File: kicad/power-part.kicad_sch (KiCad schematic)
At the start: 53 parts, among them Q10 BSS84, Q11 BSS123N, Q12 ZXMP10A17GTA, Q2 IPT012N08N5, Q3 IPT012N08N5, Q4 IPT012N08N5, Q5 IPT012N08N5, Q6 IPT012N08N5, Q7 IPT012N08N5, Q8 IPT012N08N5, Q9 IPT012N08N5

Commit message: Update files to KiCad v8
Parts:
- RT1, RT2: LCSC (none) -> C406719

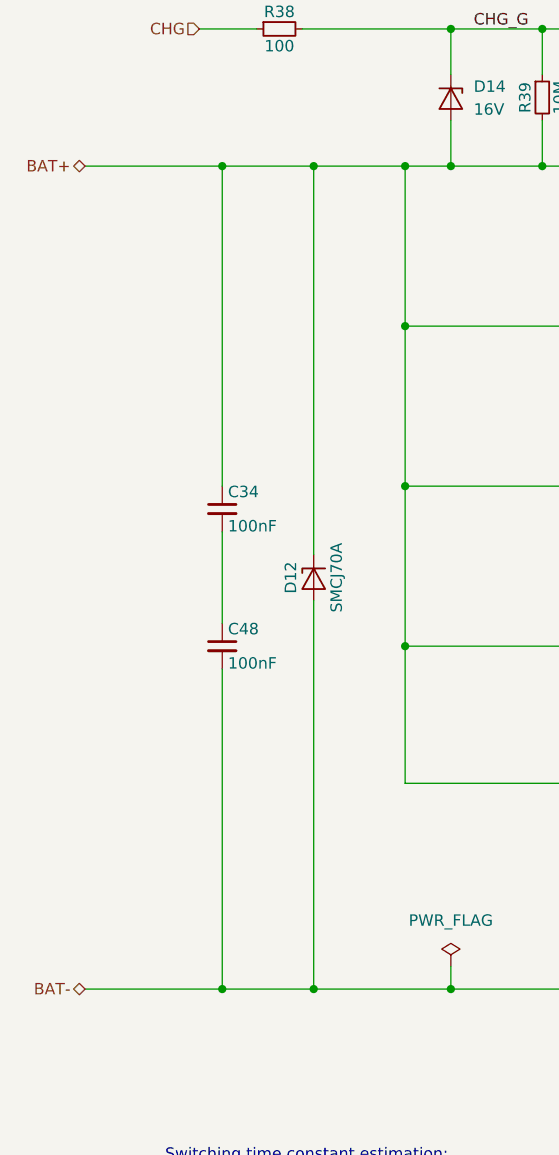
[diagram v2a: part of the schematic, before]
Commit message: changes done by jc-efactory: capacitor integrated, a 10mm SMD electrolitic footprint to test fix for issue #68, update to Kicad V9, rerouting, like the 3V3 plane was removed, now a GND layer as well and had to change a couple of capacitor to be able to fit the changes without any major redesign.
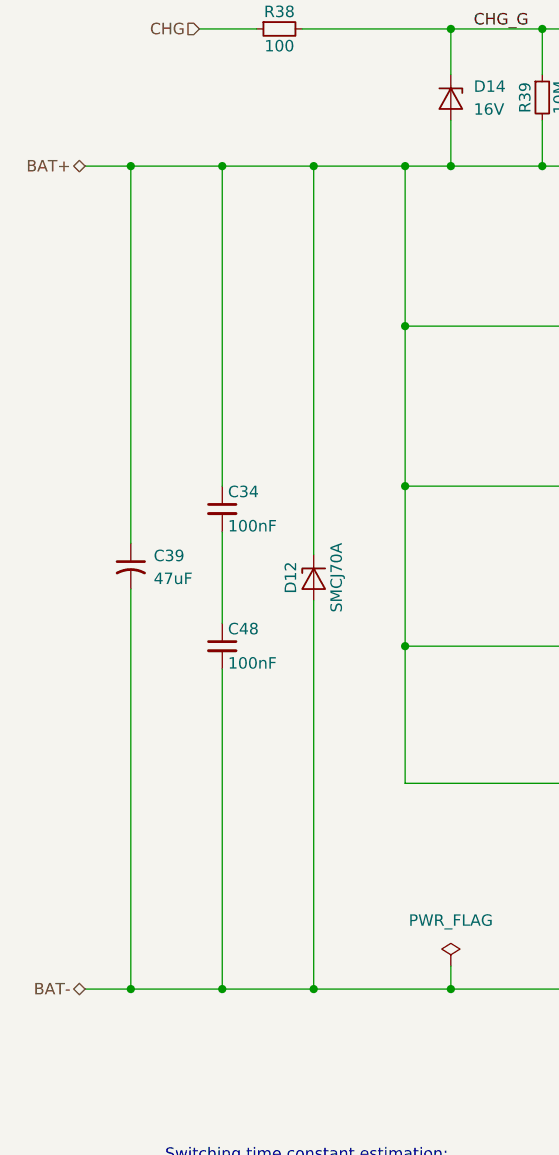
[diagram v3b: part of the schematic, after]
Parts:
- added C39: 47uF, Capacitor_SMD:CP_Elec_10x10, symbol Device:C_Small_US
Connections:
- net BAT+: now also C39.1
- net BAT-: now also C39.2
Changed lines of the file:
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@@
 (kicad_sch
-	(version 20231120)
+	(version 20250114)
 	(generator "eeschema")
-	(generator_version "8.0")
+	(generator_version "9.0")
 	(paper "A4")
 	(title_block
@@
 		(comment 3 "License: CERN-OHL-W")
 	)
+	(text "Protection against\ncharger with \nreversed polarity"
+		(exclude_from_sim no)
+		(at 208.28 26.67 0)
+		(effects
+			(font
+				(size 1.27 1.27)
+			)
+			(justify left bottom)
+		)
+	)
+	(text "Switching time constant estimation:\n- 4x IPT015N10N5 with C_iss = 16nF: 64nF\n- Gate resistor: 47R\n- Time constant: R*C = 3us"
+		(exclude_from_sim no)
+		(at 36.83 185.42 0)
+		(effects
+			(font
+				(size 1.27 1.27)
+			)
+			(justify left bottom)
+		)
+	)
+	(text "MOSFETs and Shunt"
+		(exclude_from_sim no)
+		(at 34.29 33.02 0)
+		(effects
+			(font
+				(size 2.54 2.54)
+			)
+			(justify left bottom)
+		)
+	)
+	(text "Local turn-off \ncircuit for higher\nspeed/current"
+		(exclude_from_sim no)
+		(at 182.88 26.67 0)
+		(effects
+			(font
+				(size 1.27 1.27)
+			)
+			(justify left bottom)
+		)
+	)
+	(text "Bus precharge circuit"
+		(exclude_from_sim no)
+		(at 187.96 86.36 0)
+		(effects
+			(font
+				(size 2.54 2.54)
+			)
+			(justify left bottom)
+		)
+	)
+	(text "Calculations:\n- Peak current: 60V / 40R = 1.5A\n- Time constant for C_bus 5mF: 0.2s\n- Dissipated energy: 9J\n\nShort circuit must be detected and\ninterrupted within <100 ms to\navoid overloading of the resistor.\n\nMax. continuous current: 0.5 A"
+		(exclude_from_sim no)
+		(at 187.96 149.86 0)
+		(effects
+			(font
+				(size 1.27 1.27)
+			)
+			(justify left bottom)
+		)
+	)
 	(junction
 		(at 116.84 68.58)
@@
 	)
 	(junction
+		(at 33.02 68.58)
+		(diameter 0)
+		(color 0 0 0 0)
+	)
+	(junction
 		(at 180.34 93.98)
 		(diameter 0)
@@
 	)
 	(junction
+		(at 33.02 160.02)
+		(diameter 0)
+		(color 0 0 0 0)
+	)
+	(junction
 		(at 190.5 109.22)
 		(diameter 0)
@@
 	(wire
 		(pts
+			(xy 33.02 68.58) (xy 33.02 110.49)
+		)
+		(stroke
+			(width 0)
+			(type default)
+		)
+	)
+	(wire
+		(pts
 			(xy 68.58 68.58) (xy 78.74 68.58)
 		)
@@
 	(wire
 		(pts
+			(xy 33.02 160.02) (xy 43.18 160.02)
+		)
+		(stroke
+			(width 0.508)
+			(type default)
+		)
+	)
+	(wire
+		(pts
 			(xy 63.5 104.14) (xy 63.5 121.92)
 		)
@@
 	(wire
 		(pts
+			(xy 33.02 115.57) (xy 33.02 160.02)
+		)
+		(stroke
+			(width 0)
+			(type default)
+		)
+	)
+	(wire
+		(pts
+			(xy 33.02 68.58) (xy 43.18 68.58)
+		)
+		(stroke
+			(width 0.508)
+			(type default)
+		)
+	)
+	(wire
+		(pts
 			(xy 172.72 53.34) (xy 177.8 53.34)
 		)
@@
 	(wire
 		(pts
-			(xy 27.94 68.58) (xy 43.18 68.58)
+			(xy 27.94 68.58) (xy 33.02 68.58)
 		)
 		(stroke
@@
 	(wire
 		(pts
-			(xy 27.94 160.02) (xy 43.18 160.02)
+			(xy 27.94 160.02) (xy 33.02 160.02)
 		)
 		(stroke
@@
 		)
 	)
-	(text "Protection against\ncharger with \nreversed polarity"
-		(exclude_from_sim no)
-		(at 208.28 26.67 0)
-		(effects
-			(font
-				(size 1.27 1.27)
-			)
-			(justify left bottom)
-		)
-	)
-	(text "Switching time constant estimation:\n- 4x IPT015N10N5 with C_iss = 16nF: 64nF\n- Gate resistor: 47R\n- Time constant: R*C = 3us"
-		(exclude_from_sim no)
-		(at 36.83 185.42 0)
-		(effects
-			(font
-				(size 1.27 1.27)
-			)
-			(justify left bottom)
-		)
-	)
-	(text "MOSFETs and Shunt"
-		(exclude_from_sim no)
-		(at 34.29 33.02 0)
-		(effects
-			(font
-				(size 2.54 2.54)
-			)
-			(justify left bottom)
-		)
-	)
-	(text "Local turn-off \ncircuit for higher\nspeed/current"
-		(exclude_from_sim no)
-		(at 182.88 26.67 0)
-		(effects
-			(font
-				(size 1.27 1.27)
-			)
-			(justify left bottom)
-		)
-	)
-	(text "Bus precharge circuit"
-		(exclude_from_sim no)
-		(at 187.96 86.36 0)
-		(effects
-			(font
-				(size 2.54 2.54)
-			)
-			(justify left bottom)
-		)
-	)
-	(text "Calculations:\n- Peak current: 60V / 40R = 1.5A\n- Time constant for C_bus 5mF: 0.2s\n- Dissipated energy: 9J\n\nShort circuit must be detected and\ninterrupted within <100 ms to\navoid overloading of the resistor.\n\nMax. continuous current: 0.5 A"
-		(exclude_from_sim no)
-		(at 187.96 149.86 0)
-		(effects
-			(font
-				(size 1.27 1.27)
-			)
-			(justify left bottom)
-		)
-	)
 	(label "PACK-"
 		(at 238.76 22.86 270)
-		(fields_autoplaced yes)
 		(effects
 			(font
@@
 	(label "DSG_G"
 		(at 195.58 43.18 0)
-		(fields_autoplaced yes)
 		(effects
 			(font
@@
 	(label "CHG_G"
 		(at 71.12 53.34 0)
-		(fields_autoplaced yes)
 		(effects
 			(font
@@
 		(shape input)
 		(at 101.6 27.94 180)
-		(fields_autoplaced yes)
 		(effects
 			(font
@@
 		(shape input)
 		(at 175.26 93.98 180)
-		(fields_autoplaced yes)
 		(effects
 			(font
@@
 		(shape input)
 		(at 40.64 53.34 180)
-		(fields_autoplaced yes)
 		(effects
 			(font
@@
 		(shape output)
 		(at 124.46 172.72 0)
-		(fields_autoplaced yes)
 		(effects
 			(font
@@
 		(shape bidirectional)
 		(at 27.94 68.58 180)
-		(fields_autoplaced yes)
 		(effects
 			(font
@@
 		(shape output)
 		(at 124.46 154.94 90)
-		(fields_autoplaced yes)
 		(effects
 			(font
@@
 		(shape bidirectional)
 		(at 175.26 119.38 180)
-		(fields_autoplaced yes)
 		(effects
 			(font
@@
 		(shape bidirectional)
 		(at 269.24 68.58 0)
-		(fields_autoplaced yes)
 		(effects
 			(font
@@
 		(shape bidirectional)
 		(at 27.94 160.02 180)
-		(fields_autoplaced yes)
 		(effects
 			(font
@@
 		(shape bidirectional)
 		(at 106.68 63.5 90)
-		(fields_autoplaced yes)
 		(effects
 			(font
@@
 		(shape bidirectional)
 		(at 269.24 160.02 0)
-		(fields_autoplaced yes)
 		(effects
 			(font
@@
 		(shape bidirectional)
 		(at 236.22 119.38 0)
-		(fields_autoplaced yes)
 		(effects
 			(font
@@
 		(shape output)
 		(at 119.38 154.94 90)
-		(fields_autoplaced yes)
 		(effects
 			(font
@@
 		(shape output)
 		(at 99.06 38.1 0)
-		(fields_autoplaced yes)
 		(effects
 			(font
@@
 					(unit 1)
 				)
+			)
+		)
+	)
+	(symbol
+		(lib_id "Device:C_Small_US")
+		(at 33.02 113.03 0)
+		(unit 1)
+		(exclude_from_sim no)
+		(in_bom yes)
+		(on_board yes)
+		(dnp no)
+		(fields_autoplaced yes)
+		(property "Reference" "C39"
+			(at 35.56 111.8869 0)
+			(effects
+				(font
+					(size 1.27 1.27)
+				)
+				(justify left)
+			)
+		)
+		(property "Value" "47uF"
+			(at 35.56 114.4269 0)
+			(effects
+				(font
+					(size 1.27 1.27)
+				)
+				(justify left)
+			)
+		)
+		(property "Footprint" "Capacitor_SMD:CP_Elec_10x10"
+			(at 33.02 113.03 0)
+			(effects
+				(font
+					(size 1.27 1.27)
+				)
+				(hide yes)
+			)
+		)
+		(property "Datasheet" ""
+			(at 33.02 113.03 0)
+			(effects
+				(font
+					(size 1.27 1.27)
+				)
+				(hide yes)
+			)
+		)
+		(property "Description" ""
+			(at 33.02 113.03 0)
+			(effects
+				(font
+					(size 1.27 1.27)
+				)
+				(hide yes)
+			)
+		)
+		(property "Remarks" "min. 100V"
+			(at 33.02 113.03 0)
+			(effects
+				(font
+					(size 1.27 1.27)
+				)
+				(hide yes)
+			)
+		)
+		(property "Manufacturer" "KYOCERA AVX"
+			(at 33.02 113.03 0)
+			(effects
+				(font
+					(size 1.27 1.27)
+				)
+				(hide yes)
+			)
+		)
+		(property "PartNumber" "AEK1010470M100R"
+			(at 33.02 113.03 0)
+			(effects
+				(font
+					(size 1.27 1.27)
+				)
+				(hide yes)
+			)
+		)
+		(pin "2"
+		)
+		(pin "1"
+		)
+		(instances
+			(project ""
+				(path "/5335aa43-6e7e-459f-9425-0b3d35652705/1a7f6efa-ef60-433d-acc0-6f9a9126bc57"
+					(reference "C39")
+					(unit 1)
+				)
